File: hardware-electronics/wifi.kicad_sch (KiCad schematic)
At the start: 16 parts, among them J4 CONMHF1-SMD-T, U1 RTL8188FTV-VC-CG, Y5 ABM8-40.000MHZ-B2-T

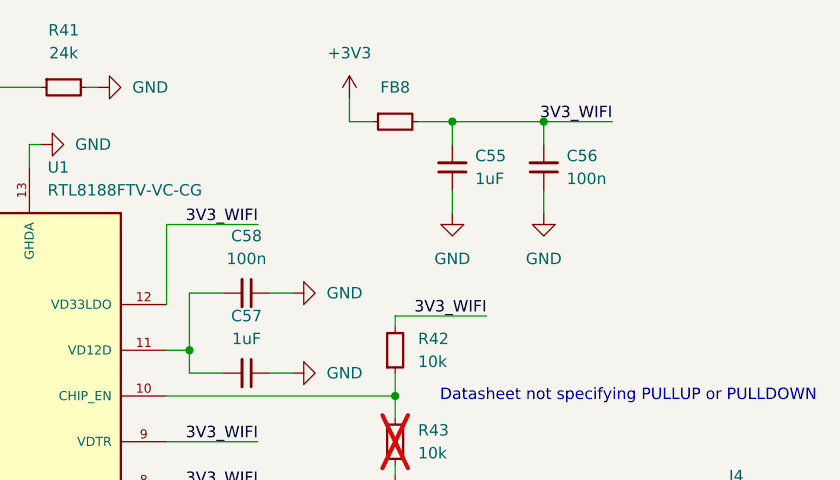
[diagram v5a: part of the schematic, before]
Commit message: [#9] SCH wifi replace power symbols
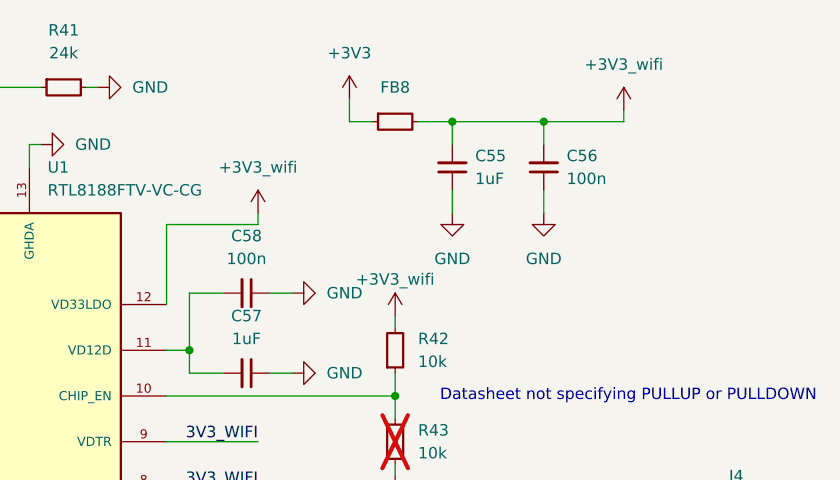
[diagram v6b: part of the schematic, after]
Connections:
- net 3V3_WIFI: no longer C55.2, C56.2, FB8.2, R42.2, U1.12 (VD33LDO)
- new net +3V3_wifi: C55.2, C56.2, FB8.2, R42.2, U1.12 (VD33LDO)
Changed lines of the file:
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@@
+	(wire
+		(pts
+			(xy 223.52 63.5) (xy 223.52 62.23)
+		)
+		(stroke
+			(width 0)
+			(type default)
+		)
+	)
 	(wire
 		(pts
@@
 	(wire
 		(pts
-			(xy 198.12 85.09) (xy 208.28 85.09)
-		)
-		(stroke
-			(width 0)
-			(type default)
-		)
-	)
-	(wire
-		(pts
 			(xy 163.83 59.69) (xy 165.1 59.69)
 		)
@@
 	(wire
 		(pts
+			(xy 182.88 73.66) (xy 182.88 74.93)
+		)
+		(stroke
+			(width 0)
+			(type default)
+		)
+	)
+	(wire
+		(pts
 			(xy 204.47 63.5) (xy 214.63 63.5)
 		)
@@
 	(wire
 		(pts
-			(xy 214.63 63.5) (xy 222.25 63.5)
+			(xy 214.63 63.5) (xy 223.52 63.5)
 		)
 		(stroke
@@
 		)
 	)
-	(label "3V3_WIFI"
-		(at 208.28 85.09 180)
+	(label "XTAL2"
+		(at 137.16 132.08 90)
 		(fields_autoplaced yes)
 		(effects
@@
 				(size 1.27 1.27)
 			)
-			(justify right bottom)
+			(justify left bottom)
 		)
 	)
 	(label "3V3_WIFI"
-		(at 222.25 63.5 180)
+		(at 132.08 134.62 90)
 		(fields_autoplaced yes)
 		(effects
@@
 				(size 1.27 1.27)
 			)
-			(justify right bottom)
-		)
-	)
-	(label "XTAL2"
-		(at 137.16 132.08 90)
-		(fields_autoplaced yes)
-		(effects
-			(font
-				(size 1.27 1.27)
-			)
-			(justify left bottom)
-		)
-	)
-	(label "3V3_WIFI"
-		(at 132.08 134.62 90)
-		(fields_autoplaced yes)
-		(effects
-			(font
-				(size 1.27 1.27)
-			)
 			(justify left bottom)
 		)
@@
 	(label "3V3_WIFI"
 		(at 132.08 58.42 270)
-		(fields_autoplaced yes)
-		(effects
-			(font
-				(size 1.27 1.27)
-			)
-			(justify right bottom)
-		)
-	)
-	(label "3V3_WIFI"
-		(at 182.88 74.93 180)
 		(fields_autoplaced yes)
 		(effects
@@
 				(path "/da663dec-9e91-4003-a791-431d460ad63c/7a341d5c-2113-408f-a1b4-1e4771333f4d"
 					(reference "#PWR0131")
+					(unit 1)
+				)
+			)
+		)
+	)
+	(symbol
+		(lib_id "power:+3V3")
+		(at 198.12 85.09 0)
+		(unit 1)
+		(exclude_from_sim no)
+		(in_bom yes)
+		(on_board yes)
+		(dnp no)
+		(property "Reference" "#PWR0166"
+			(at 198.12 88.9 0)
+			(effects
+				(font
+					(size 1.27 1.27)
+				)
+				(hide yes)
+			)
+		)
+		(property "Value" "+3V3_wifi"
+			(at 198.12 81.026 0)
+			(effects
+				(font
+					(size 1.27 1.27)
+				)
+			)
+		)
+		(property "Footprint" ""
+			(at 198.12 85.09 0)
+			(effects
+				(font
+					(size 1.27 1.27)
+				)
+				(hide yes)
+			)
+		)
+		(property "Datasheet" ""
+			(at 198.12 85.09 0)
+			(effects
+				(font
+					(size 1.27 1.27)
+				)
+				(hide yes)
+			)
+		)
+		(property "Description" "Power symbol creates a global label with name \"+3V3\""
+			(at 198.12 85.09 0)
+			(effects
+				(font
+					(size 1.27 1.27)
+				)
+				(hide yes)
+			)
+		)
+		(pin "1"
+		)
+		(instances
+			(project "M2SmartHome"
+				(path "/da663dec-9e91-4003-a791-431d460ad63c/7a341d5c-2113-408f-a1b4-1e4771333f4d"
+					(reference "#PWR0166")
 					(unit 1)
 				)
@@
 	)
 	(symbol
+		(lib_id "power:+3V3")
+		(at 182.88 73.66 0)
+		(unit 1)
+		(exclude_from_sim no)
+		(in_bom yes)
+		(on_board yes)
+		(dnp no)
+		(fields_autoplaced yes)
+		(property "Reference" "#PWR0165"
+			(at 182.88 77.47 0)
+			(effects
+				(font
+					(size 1.27 1.27)
+				)
+				(hide yes)
+			)
+		)
+		(property "Value" "+3V3_wifi"
+			(at 182.88 68.58 0)
+			(effects
+				(font
+					(size 1.27 1.27)
+				)
+			)
+		)
+		(property "Footprint" ""
+			(at 182.88 73.66 0)
+			(effects
+				(font
+					(size 1.27 1.27)
+				)
+				(hide yes)
+			)
+		)
+		(property "Datasheet" ""
+			(at 182.88 73.66 0)
+			(effects
+				(font
+					(size 1.27 1.27)
+				)
+				(hide yes)
+			)
+		)
+		(property "Description" "Power symbol creates a global label with name \"+3V3\""
+			(at 182.88 73.66 0)
+			(effects
+				(font
+					(size 1.27 1.27)
+				)
+				(hide yes)
+			)
+		)
+		(pin "1"
+		)
+		(instances
+			(project "M2SmartHome"
+				(path "/da663dec-9e91-4003-a791-431d460ad63c/7a341d5c-2113-408f-a1b4-1e4771333f4d"
+					(reference "#PWR0165")
+					(unit 1)
+				)
+			)
+		)
+	)
+	(symbol
 		(lib_id "power:GND")
 		(at 214.63 73.66 0)
@@
 					(unit 1)
 				)
+			)
+		)
+	)
+	(symbol
+		(lib_id "power:+3V3")
+		(at 223.52 62.23 0)
+		(unit 1)
+		(exclude_from_sim no)
+		(in_bom yes)
+		(on_board yes)
+		(dnp no)
+		(fields_autoplaced yes)
+		(property "Reference" "#PWR0163"
+			(at 223.52 66.04 0)
+			(effects
+				(font
+					(size 1.27 1.27)
+				)
+				(hide yes)
+			)
+		)
+		(property "Value" "+3V3_wifi"
+			(at 223.52 57.15 0)
+			(effects
+				(font
+					(size 1.27 1.27)
+				)
+			)
+		)
+		(property "Footprint" ""
+			(at 223.52 62.23 0)
+			(effects
+				(font
+					(size 1.27 1.27)
+				)
+				(hide yes)
+			)
+		)
+		(property "Datasheet" ""
+			(at 223.52 62.23 0)
+			(effects
+				(font
+					(size 1.27 1.27)
+				)
+				(hide yes)
+			)
+		)
+		(property "Description" "Power symbol creates a global label with name \"+3V3\""
+			(at 223.52 62.23 0)
+			(effects
+				(font
+					(size 1.27 1.27)
+				)
+				(hide yes)
+			)
+		)
+		(pin "1"
+		)
+		(instances
+			(project "M2SmartHome"
+				(path "/da663dec-9e91-4003-a791-431d460ad63c/7a341d5c-2113-408f-a1b4-1e4771333f4d"
+					(reference "#PWR0163")
+					(unit 1)
+				)

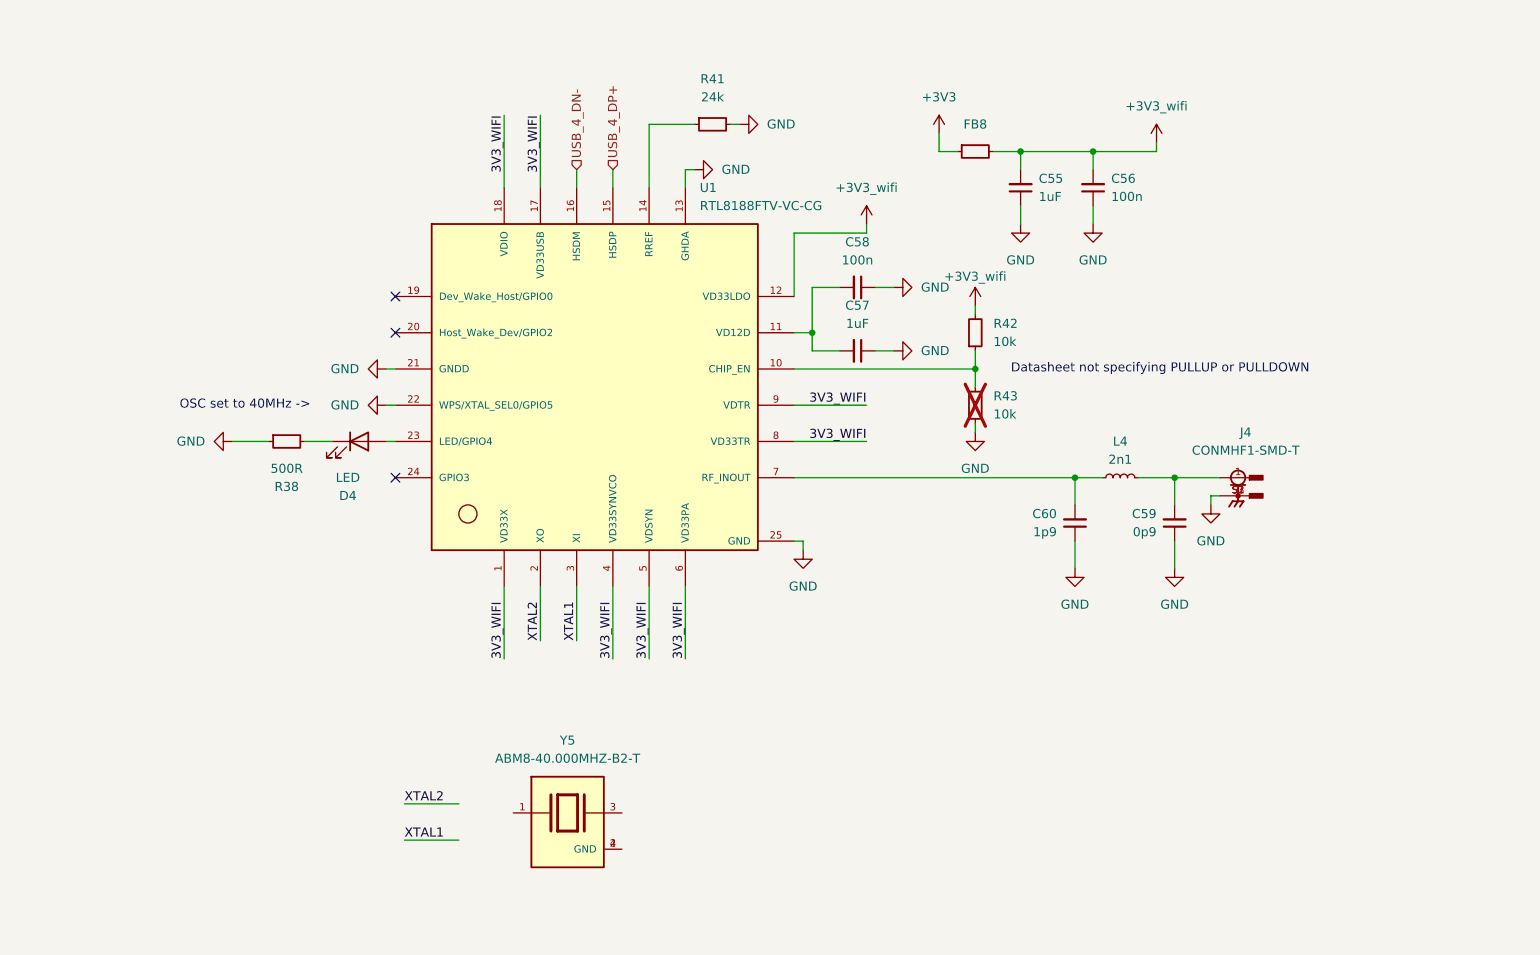
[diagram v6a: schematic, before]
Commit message: [#9] SCH wifi connected crystal oscillator
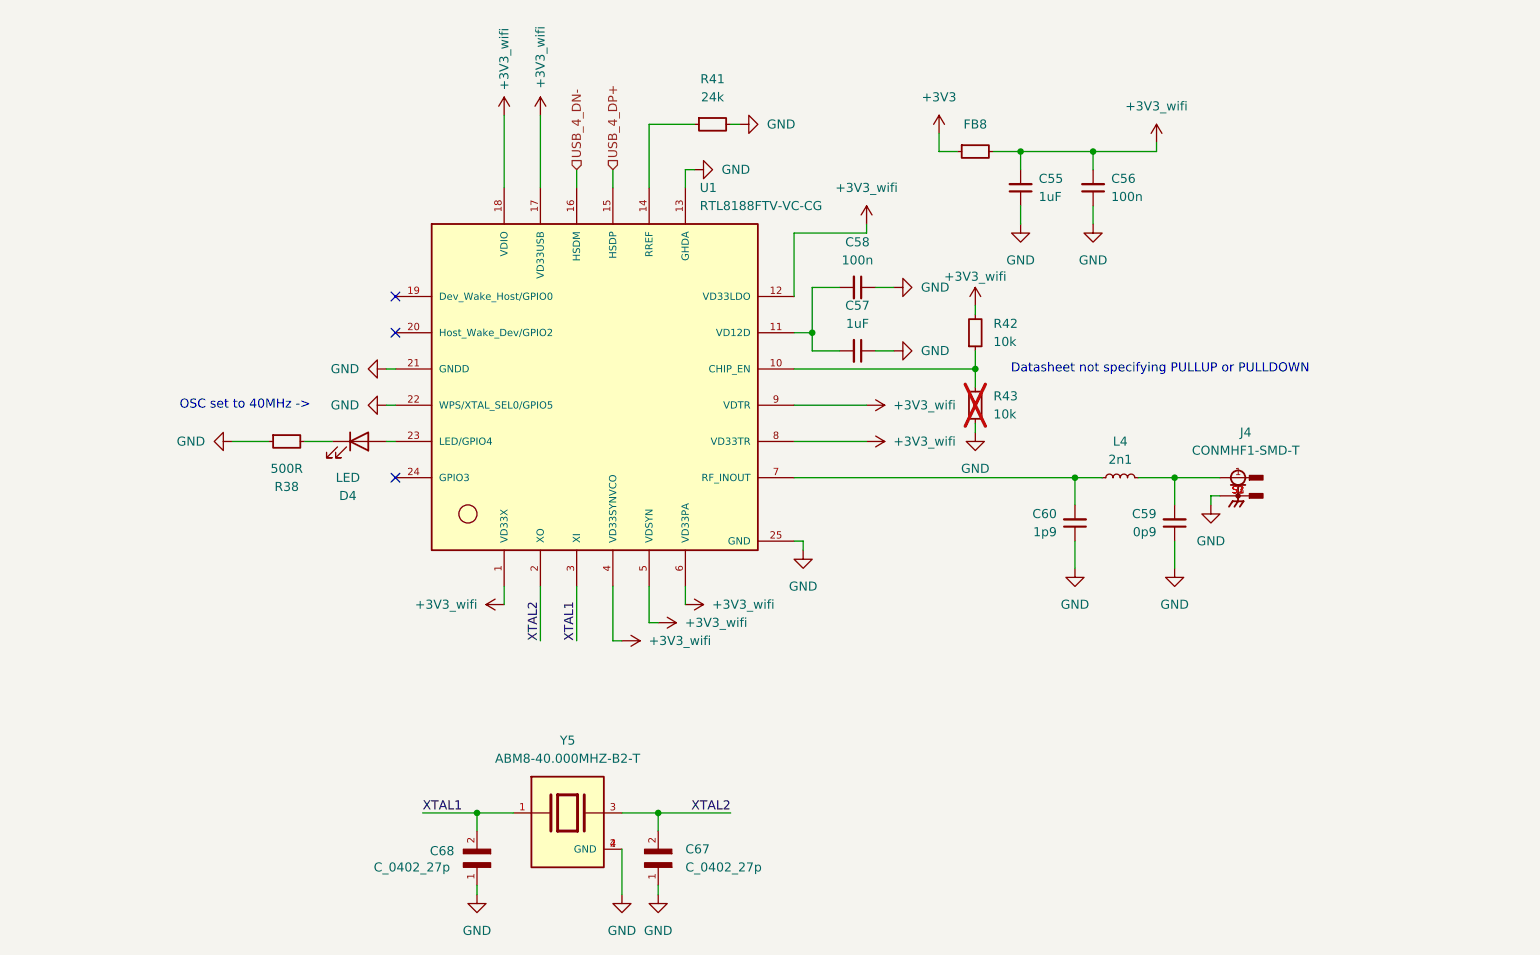
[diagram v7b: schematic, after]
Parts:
- added C67, C68: C_0402_27p, M2SmartHomeFootprints:C_0402, symbol M2SmartHomeSymbols:04025A270FAT2A
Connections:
- net 3V3_WIFI is gone; now on net +3V3_wifi: U1.1 (VD33X), U1.17 (VD33USB), U1.18 (VDIO), U1.4 (VD33SYNVCO), U1.5 (VDSYN), U1.6 (VD33PA), U1.8 (VD33TR), U1.9 (VDTR)
- net GND: now also Y5.2 (GND), Y5.4 (GND), C67.1, C68.1
- net XTAL1: now also Y5.1, C68.2
- net XTAL2: now also Y5.3, C67.2

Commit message: SCH cosmetic changes
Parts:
- added C75, C77: C_1uF_0402, C_1uF_0402:C_0402_1005Metric, symbol M2SmartHomeSymbols:C_1uF_0402
- added C76, C78: C_100n_0402, C_100n_0402:C_0402_1005Metric, symbol M2SmartHomeSymbols:C_100n_0402
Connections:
- net +3V3_wifi: now also C75.2, C76.2, C77.2, C78.2
- net GND: now also C75.1, C76.1, C77.1, C78.1
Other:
- note added: "Datasheet not specyfing PULLUP or PULLDOWN"
- note removed: "Datasheet not specifying PULLUP or PULLDOWN"
- moved on the sheet: C55, C56, FB8, R42, R43
